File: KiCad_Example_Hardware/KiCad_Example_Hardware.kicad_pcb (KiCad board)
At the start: 4 copper layers, 76.2 x 101.6 mm, 104 parts, among them J1 RJ45_LED_Shielded, Q1 SI4156DY, Q10 SI4156DY, Q11 SI4156DY, Q12 SI4156DY, Q13 SI4156DY, Q14 SI4156DY, Q15 SI4156DY, Q16 SI4156DY, Q2 SI4156DY, Q3 SI4156DY, Q4 SI4156DY, Q5 SI4156DY, Q6 SI4156DY, Q7 SI4156DY, Q8 SI4156DY, Q9 SI4156DY, U1 TSR_1-2450, U10 74LVC2G04, U11 IRS2005S, U12 IRS2005S, U13 IRS2005S, U14 IRS2005S, U2 74LVC2G04, U3 IRS2005S, U4 IRS2005S, U5 74LVC2G04, U6 IRS2005S, U7 IRS2005S, U8 Teensy4.1_DEV-16771, U9 74LVC2G04

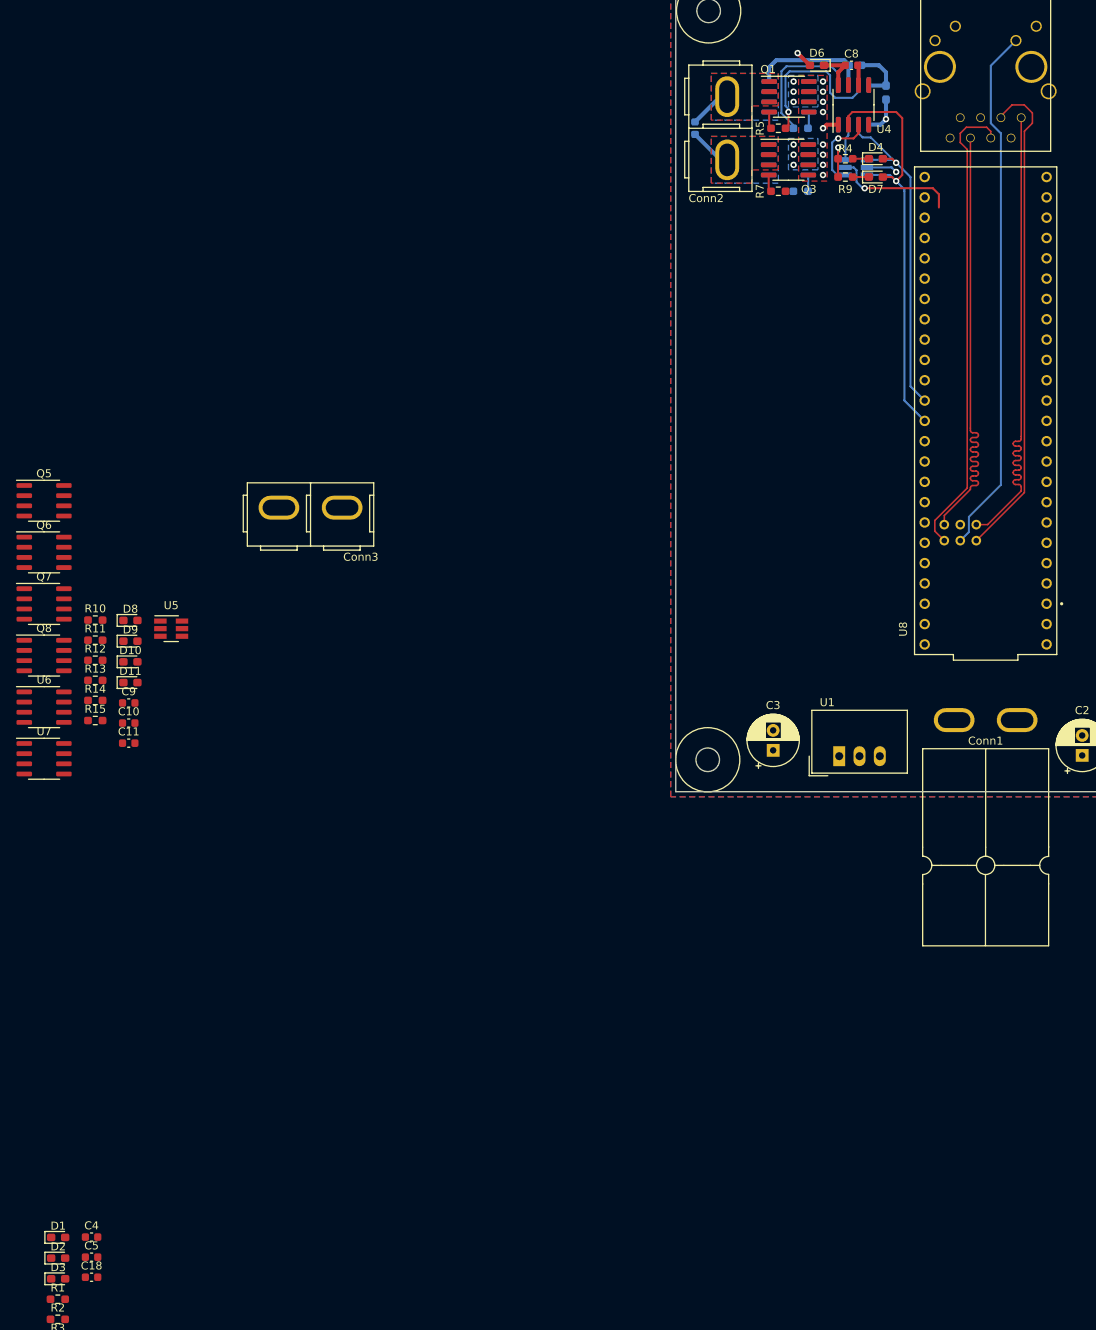
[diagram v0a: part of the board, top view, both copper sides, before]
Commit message: Finished 2nd H bridge
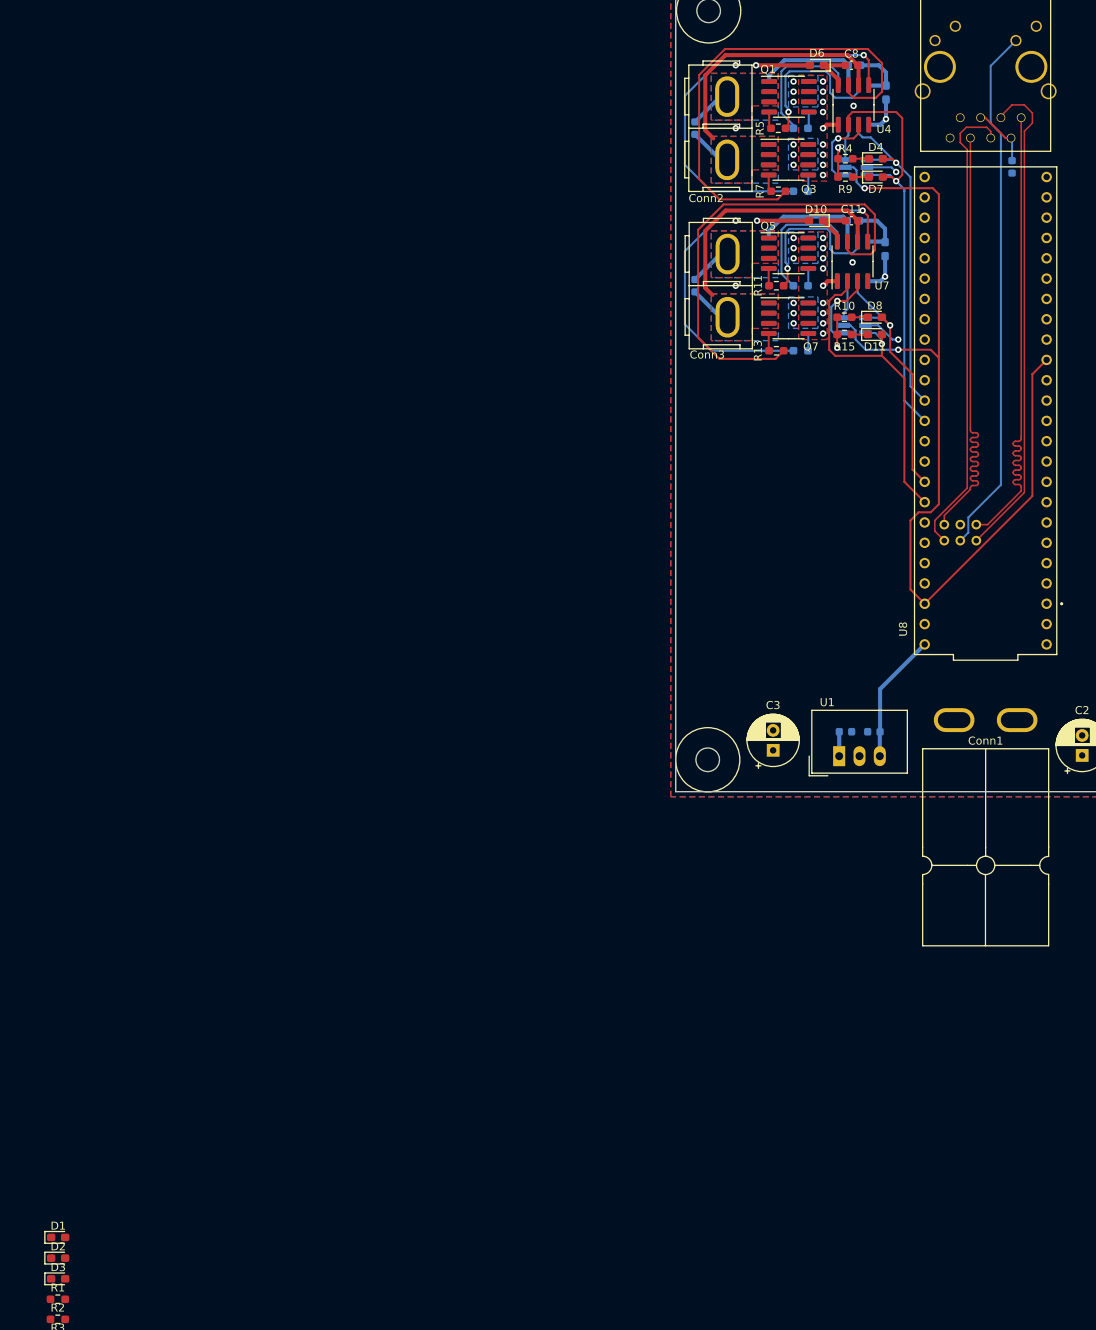
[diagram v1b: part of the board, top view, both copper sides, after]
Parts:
- C10, C18, C4, C5, C9, D9, Q6, Q8, R12, R14, U5, U6: moved to B.Cu
- moved C18 180.3 mm to (159.5, 43.2), turned to -90 degrees
- moved U7 118.7 mm to (139.6, 55.0), turned to 90 degrees
- moved C5 117.8 mm to (142.2, 113.8), turned to 180 degrees
- moved U6 115.4 mm to (139.6, 55.0), turned to 90 degrees
- moved C4 113.4 mm to (138.7, 113.8)
- moved C11 111.5 mm to (139.4, 49.9)
- moved C9 108.8 mm to (139.7, 49.9), turned to 180 degrees
- moved D9 106.3 mm to (143.6, 53.5), turned to -90 degrees
- moved R15 105.3 mm to (138.6, 64.1)
- moved D11 102.7 mm to (142.4, 64.1)
- moved Q8 102.2 mm to (131.6, 62.1), turned to 180 degrees
- moved D10 101.9 mm to (135.0, 49.9), turned to 180 degrees
- moved R10 101.0 mm to (138.6, 62.0), turned to 180 degrees
- moved D8 100.5 mm to (142.4, 62.0)
- moved Q6 100.3 mm to (131.6, 54.0), turned to 180 degrees
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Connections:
- U8 pad 18: /FWD_PWM_4 -> /FWD_PWM_2
- U8 pad 19: /RVS_PWM_4 -> /RVS_PWM_2
- U8 pad 24: /RVS_PWM_2 -> /RVS_PWM_4
- U8 pad 25: /FWD_PWM_2 -> /FWD_PWM_4
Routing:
- net +3V3: track 15.6 -> 119.3 mm, vias 1 -> 2
- net Net-(U4-HO): track 0.00 -> 59.5 mm
- net Net-(U7-HO): track 0.00 -> 59.0 mm
- net Net-(U7-LO): track 0.00 -> 52.5 mm, vias 0 -> 1
- net Net-(U4-LO): track 0.00 -> 52.0 mm, vias 0 -> 1
- net /RVS_PWM_2: track 0.00 -> 43.5 mm, vias 0 -> 1
- net /Motor Controllers/2M-: track 0.00 -> 37.0 mm
- net /FWD_PWM_2: track 0.00 -> 32.2 mm, vias 0 -> 1
- net /Motor Controllers/1M-: track 7.87 -> 36.8 mm
- net +12V: track 9.15 -> 30.2 mm, vias 11 -> 22
- net Net-(U6-HO): track 0.00 -> 19.8 mm, vias 0 -> 1
- net /Motor Controllers/2M+: track 0.00 -> 19.6 mm
- net Net-(U6-LO): track 0.00 -> 16.4 mm
- net +5V: track 0.00 -> 16.3 mm
- net Net-(U7-LIN): track 0.00 -> 9.90 mm, vias 0 -> 1
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- added copper zone on B.Cu, net /Motor Controllers/2M+
- added copper zone on F.Cu, net /Motor Controllers/2M+
- added copper zone on B.Cu, net /Motor Controllers/2M-
- added copper zone on F.Cu, net /Motor Controllers/2M-
